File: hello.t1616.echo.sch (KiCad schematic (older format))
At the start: 4 parts, among them J1 Conn_01x03_Male, J2 Conn_FTDI_01x06_Male, U1 ATtiny1616-S

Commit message: Finished (?) board
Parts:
- J1: footprint Connector_PinHeader_2.54mm:PinHeader_1x03_P2.54mm_Horizontal -> (none)
- J2: footprint Connector_PinHeader_2.54mm:PinHeader_1x06_P2.54mm_Vertical -> (none)
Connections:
- net RX: now also U1.9 (PB2); no longer U1.7 (PB4)
- net TX: now also U1.8 (PB3); no longer U1.6 (PB5)
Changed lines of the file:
@@
 F 0 "J2" H 7181 3519 50  0000 R CNN
 F 1 "Conn_FTDI_01x06_Male" H 7181 3610 50  0000 R CNN
-F 2 "Connector_PinHeader_2.54mm:PinHeader_1x06_P2.54mm_Vertical" H 7350 3600 50  0001 C CNN
+F 2 "" H 7350 3600 50  0001 C CNN
 F 3 "~" H 7350 3600 50  0001 C CNN
 	1    7350 3600
@@
 F 0 "J1" H 5708 2431 50  0000 C CNN
 F 1 "Conn_01x03_Male" H 5708 2340 50  0000 C CNN
-F 2 "Connector_PinHeader_2.54mm:PinHeader_1x03_P2.54mm_Horizontal" H 5600 2150 50  0001 C CNN
+F 2 "" H 5600 2150 50  0001 C CNN
 F 3 "~" H 5600 2150 50  0001 C CNN
 	1    5600 2150
@@
 	1    0    0    -1
 $EndComp
+Text GLabel 6250 4150 0    50   Input ~ 0
+TX
+Text GLabel 6250 4050 0    50   Output ~ 0
+RX
 Wire Wire Line
-	6000 4350 6250 4350
+	6000 4050 6250 4050
 Wire Wire Line
-	6000 4250 6250 4250
-Text GLabel 6250 4350 0    50   Input ~ 0
-TX
-Text GLabel 6250 4250 0    50   Output ~ 0
-RX
+	6000 4150 6250 4150
 $EndSCHEMATC

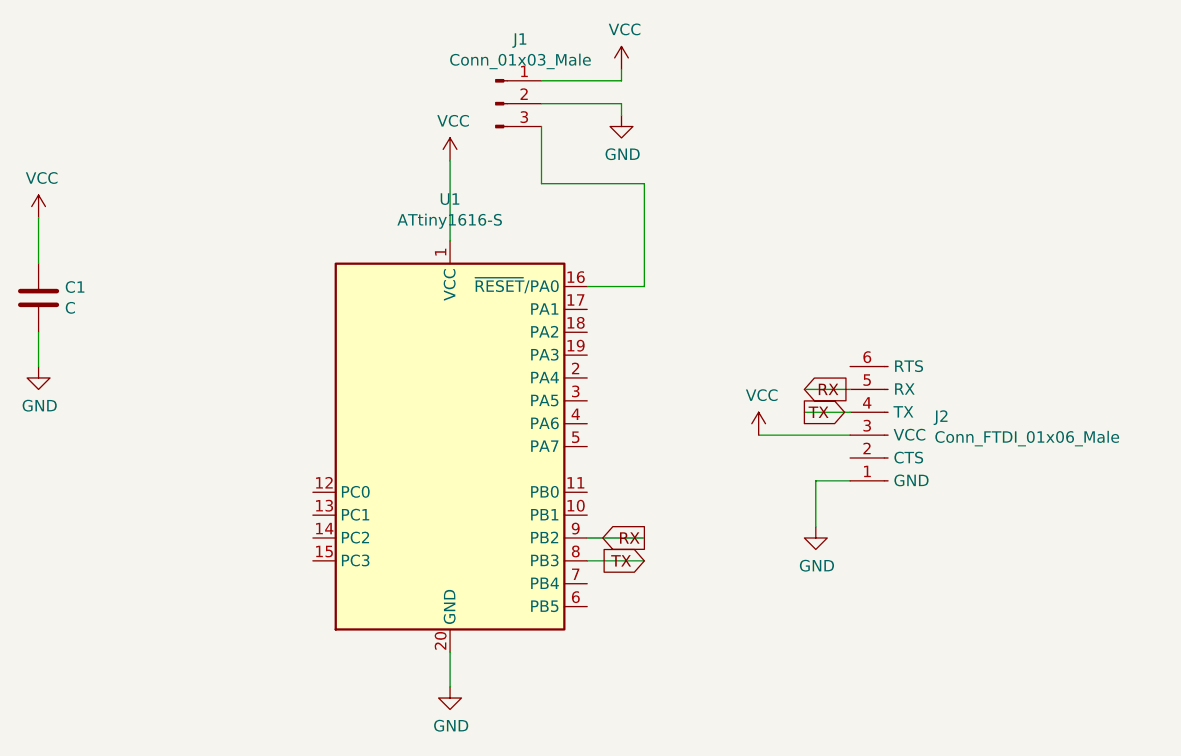
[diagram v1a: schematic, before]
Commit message: Surface mount headers, added README.
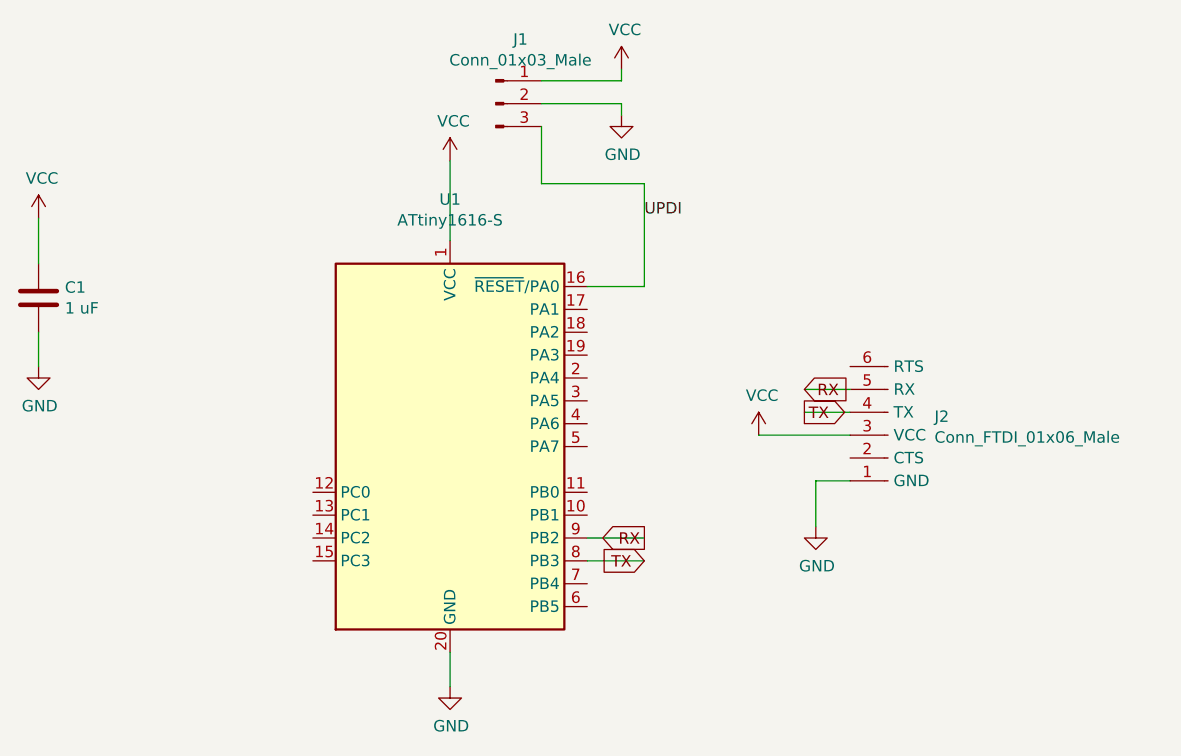
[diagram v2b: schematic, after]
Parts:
- C1: value C -> 1 uF
- J1: footprint (none) -> fab:Header_SMD_01x03_P2.54mm_Horizontal_Male
- J2: footprint (none) -> fab:Header_SMD_01x06_P2.54mm_Horizontal_Male
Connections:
- net UPDI: now reaches J1.3 (Pin_3), U1.16 (~RESET~/PA0)
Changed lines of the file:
@@
 P 3600 3000
 F 0 "C1" H 3715 3046 50  0000 L CNN
-F 1 "C" H 3715 2955 50  0000 L CNN
+F 1 "1 uF" H 3715 2955 50  0000 L CNN
 F 2 "fab:fab-C1206" H 3638 2850 50  0001 C CNN
 F 3 "" H 3600 3000 50  0001 C CNN
@@
 F 0 "J2" H 7181 3519 50  0000 R CNN
 F 1 "Conn_FTDI_01x06_Male" H 7181 3610 50  0000 R CNN
-F 2 "" H 7350 3600 50  0001 C CNN
+F 2 "fab:Header_SMD_01x06_P2.54mm_Horizontal_Male" H 7350 3600 50  0001 C CNN
 F 3 "~" H 7350 3600 50  0001 C CNN
 	1    7350 3600
@@
 F 0 "J1" H 5708 2431 50  0000 C CNN
 F 1 "Conn_01x03_Male" H 5708 2340 50  0000 C CNN
-F 2 "" H 5600 2150 50  0001 C CNN
+F 2 "fab:Header_SMD_01x03_P2.54mm_Horizontal_Male" H 5600 2150 50  0001 C CNN
 F 3 "~" H 5600 2150 50  0001 C CNN
 	1    5600 2150
@@
 Wire Wire Line
 	6000 4150 6250 4150
+Text Label 6250 2650 0    50   ~ 0
+UPDI
 $EndSCHEMATC
